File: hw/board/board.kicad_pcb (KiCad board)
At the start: 4 copper layers, 100 x 85 mm, 12 parts, among them J1 DE9_Receptacle, J2 DE9_Receptacle, J3 DE9_Receptacle, J4 DE9_Receptacle, J5 DE9_Receptacle, J6 DE9_Receptacle, J7 DE9_Receptacle, J8 DE9_Receptacle, U1 XC7A35T-FTG256

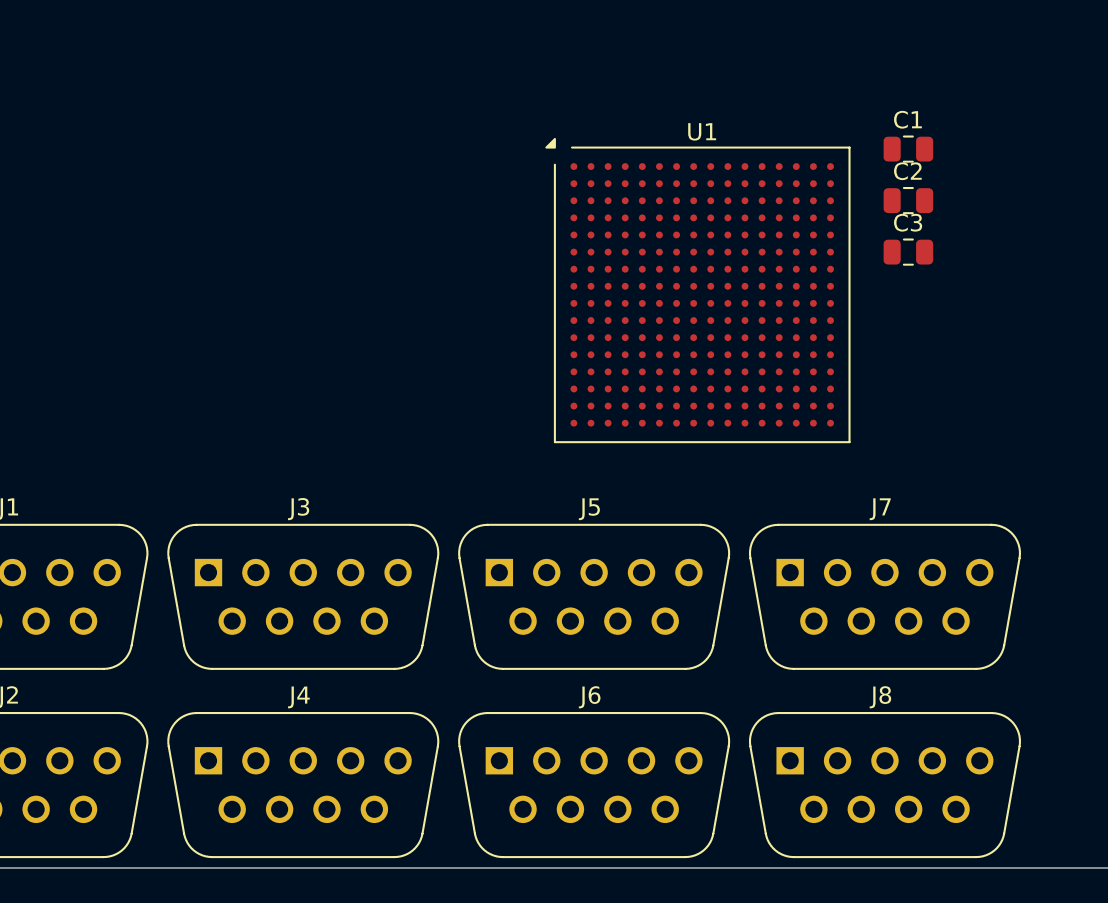
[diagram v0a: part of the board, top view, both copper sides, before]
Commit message: Added decoupling network following Xiling UG483
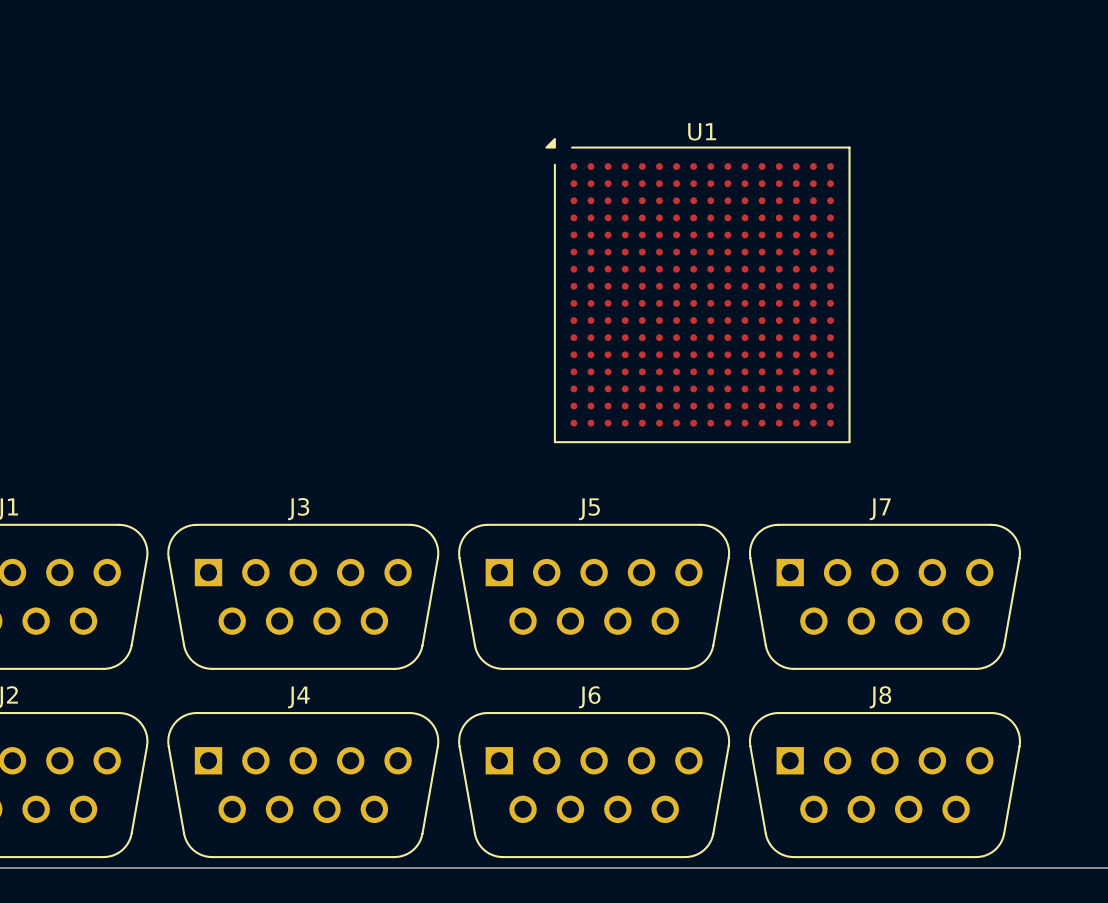
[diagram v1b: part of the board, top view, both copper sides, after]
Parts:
- removed C1, C2, C3: 10u, Capacitor_SMD:C_0805_2012Metric

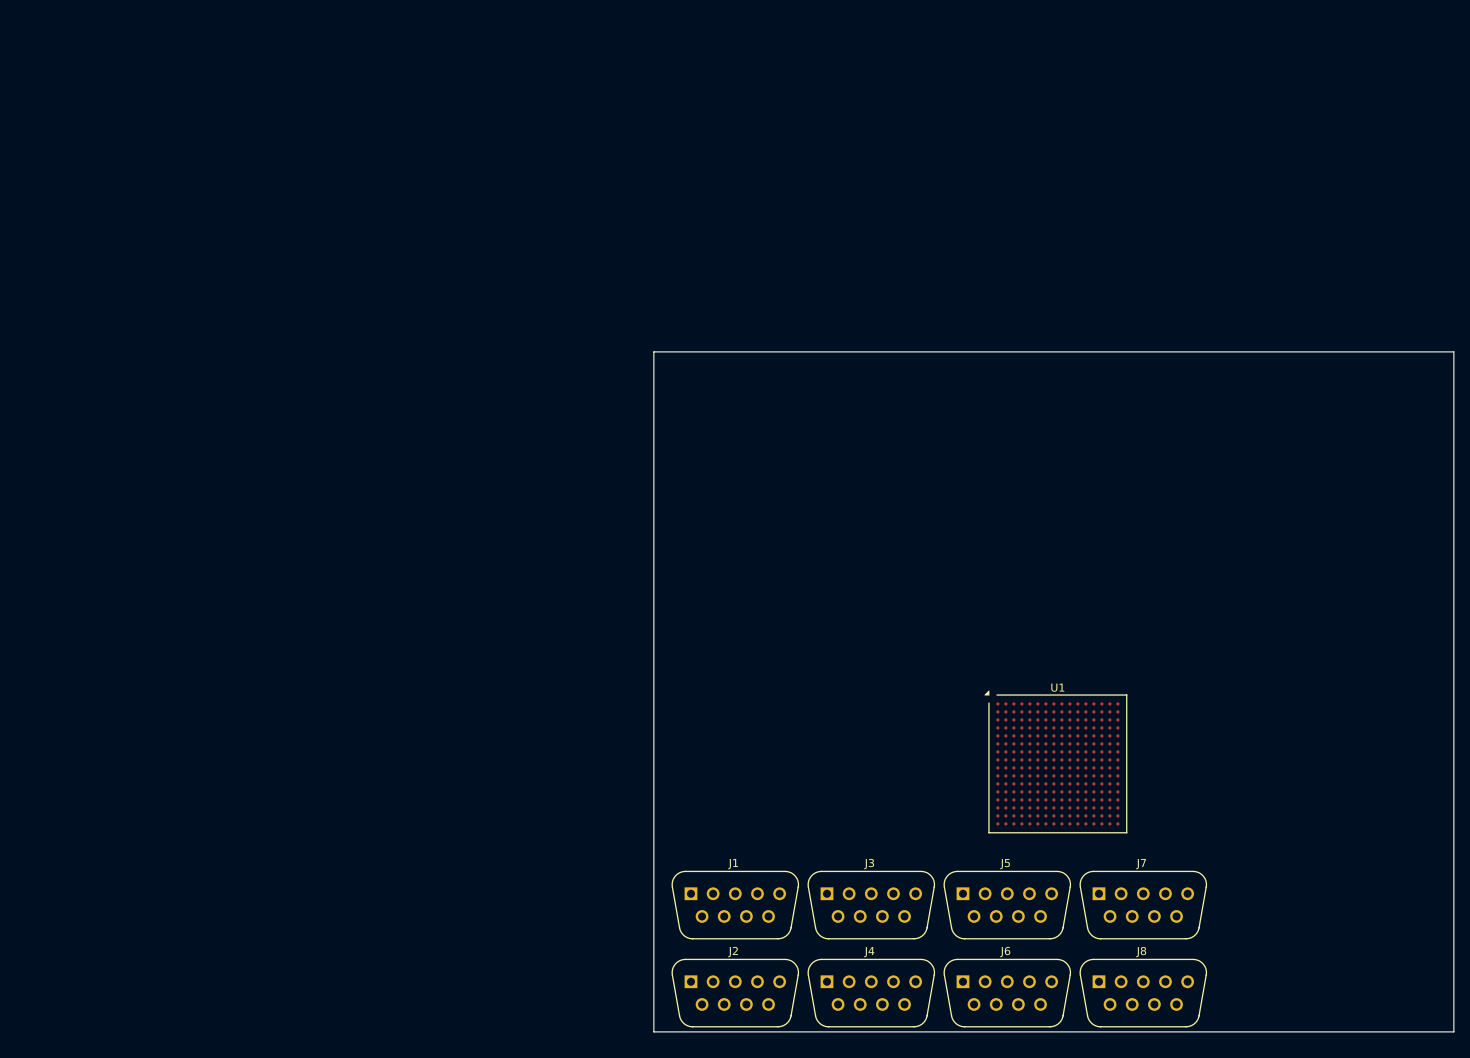
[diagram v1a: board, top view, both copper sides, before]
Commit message: Added DE9 connector footprint
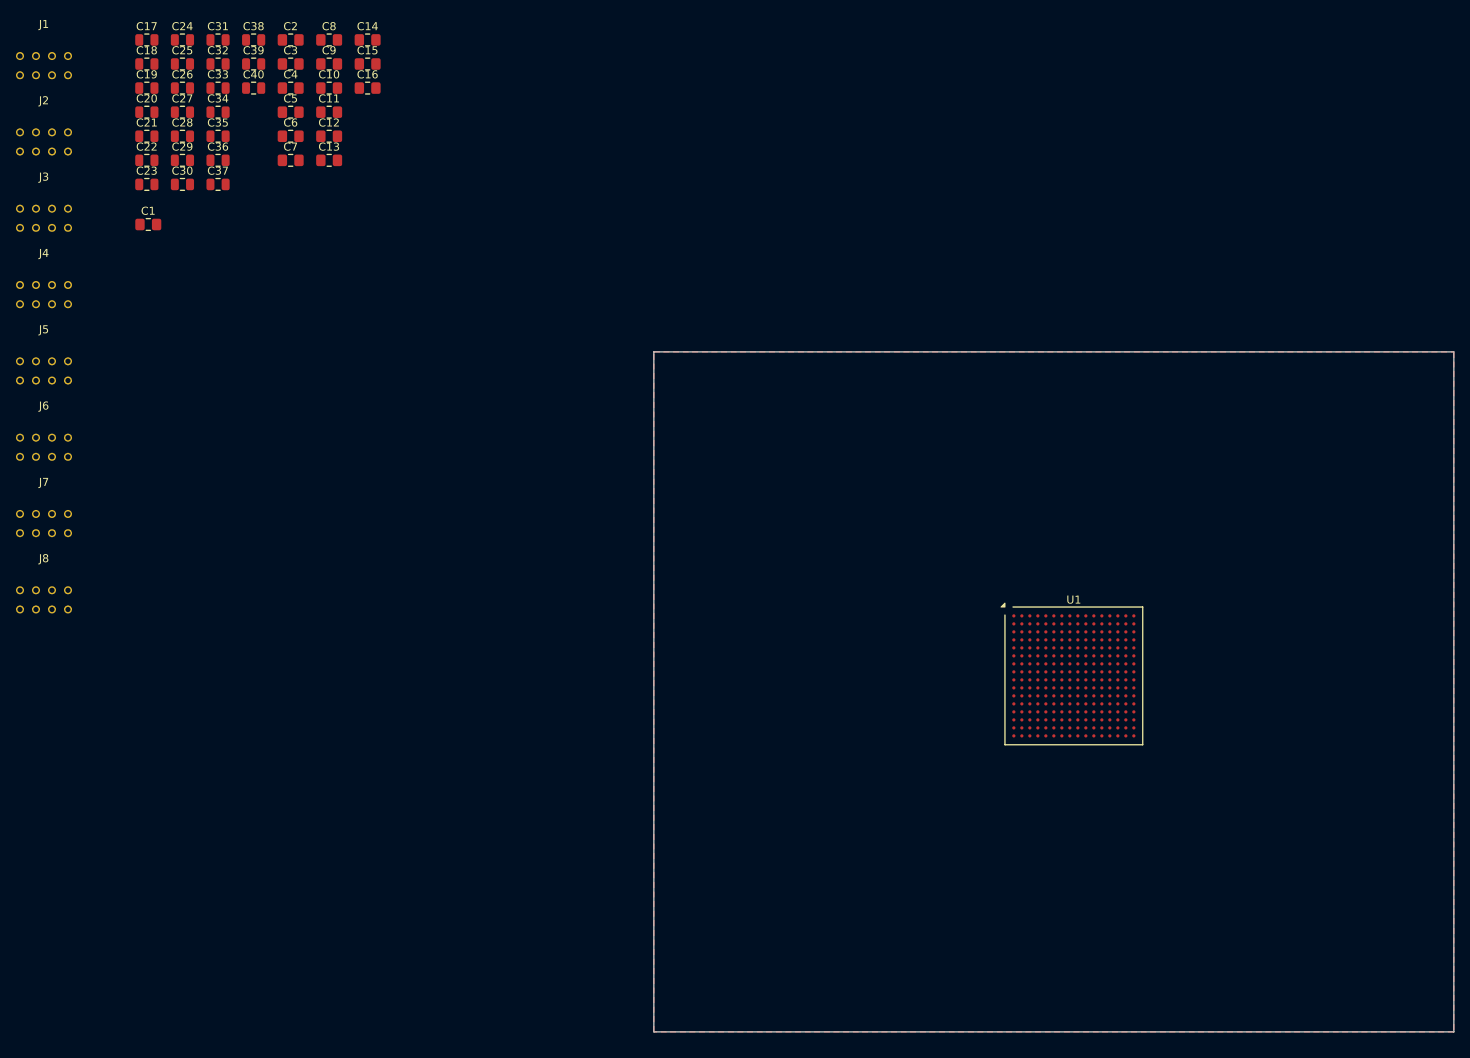
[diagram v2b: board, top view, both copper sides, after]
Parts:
- added C1: 47u, Capacitor_SMD:C_0805_2012Metric_Pad1.18x1.45mm_HandSolder, F.Cu at (20.8, 24.1)
- added C10: 100u, Capacitor_SMD:C_0805_2012Metric_Pad1.18x1.45mm_HandSolder, F.Cu at (43.4, 7.03)
- added C11: 4u7, Capacitor_SMD:C_0805_2012Metric_Pad1.18x1.45mm_HandSolder, F.Cu at (43.4, 10.0)
- added C12: 4u7, Capacitor_SMD:C_0805_2012Metric_Pad1.18x1.45mm_HandSolder, F.Cu at (43.4, 13.0)
- added C13: 470n, Capacitor_SMD:C_0805_2012Metric_Pad1.18x1.45mm_HandSolder, F.Cu at (43.4, 16.1)
- added C14: 470n, Capacitor_SMD:C_0805_2012Metric_Pad1.18x1.45mm_HandSolder, F.Cu at (48.2, 1.00)
- added C15: 470n, Capacitor_SMD:C_0805_2012Metric_Pad1.18x1.45mm_HandSolder, F.Cu at (48.2, 4.01)
- added C16: 100u, Capacitor_SMD:C_0805_2012Metric_Pad1.18x1.45mm_HandSolder, F.Cu at (48.2, 7.03)
- added C17: 470n, Capacitor_SMD:C_0805_2012Metric, F.Cu at (20.6, 1.00)
- added C18: 470n, Capacitor_SMD:C_0805_2012Metric, F.Cu at (20.6, 4.01)
- added C19: 470n, Capacitor_SMD:C_0805_2012Metric, F.Cu at (20.6, 7.03)
- added C2: 470n, Capacitor_SMD:C_0805_2012Metric_Pad1.18x1.45mm_HandSolder, F.Cu at (38.6, 1.00)
- added C20: 470n, Capacitor_SMD:C_0805_2012Metric, F.Cu at (20.6, 10.0)
- added C21: 4u7, Capacitor_SMD:C_0805_2012Metric, F.Cu at (20.6, 13.0)
- added C22: 4u7, Capacitor_SMD:C_0805_2012Metric, F.Cu at (20.6, 16.1)
- added C23: 4u7, Capacitor_SMD:C_0805_2012Metric, F.Cu at (20.6, 19.1)
- added C24: 4u7, Capacitor_SMD:C_0805_2012Metric, F.Cu at (25.1, 1.00)
- added C25: 470n, Capacitor_SMD:C_0805_2012Metric, F.Cu at (25.1, 4.01)
- added C26: 470n, Capacitor_SMD:C_0805_2012Metric, F.Cu at (25.1, 7.03)
- added C27: 470n, Capacitor_SMD:C_0805_2012Metric, F.Cu at (25.1, 10.0)
- added C28: 470n, Capacitor_SMD:C_0805_2012Metric, F.Cu at (25.1, 13.0)
- added C29: 470n, Capacitor_SMD:C_0805_2012Metric, F.Cu at (25.1, 16.1)
- added C3: 470n, Capacitor_SMD:C_0805_2012Metric_Pad1.18x1.45mm_HandSolder, F.Cu at (38.6, 4.01)
- added C30: 470n, Capacitor_SMD:C_0805_2012Metric, F.Cu at (25.1, 19.1)
- added C31: 470n, Capacitor_SMD:C_0805_2012Metric, F.Cu at (29.5, 1.00)
- added C32: 470n, Capacitor_SMD:C_0805_2012Metric, F.Cu at (29.5, 4.01)
- added C33: 4u7, Capacitor_SMD:C_0805_2012Metric, F.Cu at (29.5, 7.03)
- added C34: 4u7, Capacitor_SMD:C_0805_2012Metric, F.Cu at (29.5, 10.0)
- added C35: 4u7, Capacitor_SMD:C_0805_2012Metric, F.Cu at (29.5, 13.0)
- added C36: 4u7, Capacitor_SMD:C_0805_2012Metric, F.Cu at (29.5, 16.1)
- added C37: 470n, Capacitor_SMD:C_0805_2012Metric, F.Cu at (29.5, 19.1)
- added C38: 470n, Capacitor_SMD:C_0805_2012Metric, F.Cu at (34.0, 1.00)
- added C39: 470n, Capacitor_SMD:C_0805_2012Metric, F.Cu at (34.0, 4.01)
- added C4: 470n, Capacitor_SMD:C_0805_2012Metric_Pad1.18x1.45mm_HandSolder, F.Cu at (38.6, 7.03)
- added C40: 470n, Capacitor_SMD:C_0805_2012Metric, F.Cu at (34.0, 7.03)
- added C5: 4u7, Capacitor_SMD:C_0805_2012Metric_Pad1.18x1.45mm_HandSolder, F.Cu at (38.6, 10.0)
- added C6: 47u, Capacitor_SMD:C_0805_2012Metric_Pad1.18x1.45mm_HandSolder, F.Cu at (38.6, 13.0)
- added C7: 4u7, Capacitor_SMD:C_0805_2012Metric_Pad1.18x1.45mm_HandSolder, F.Cu at (38.6, 16.1)
- added C8: 470n, Capacitor_SMD:C_0805_2012Metric_Pad1.18x1.45mm_HandSolder, F.Cu at (43.4, 1.00)
- added C9: 47u, Capacitor_SMD:C_0805_2012Metric_Pad1.18x1.45mm_HandSolder, F.Cu at (43.4, 4.01)
- J1, J2, J3, J4, J5, J6, J7, J8: value DE9_Receptacle -> ~
- moved J8 145.8 mm to (7.77, 70.9)
- moved J7 145.3 mm to (7.77, 61.4)
- moved J6 138.2 mm to (7.77, 51.8)
- moved J5 137.5 mm to (7.77, 42.3)
- moved J2 136.9 mm to (7.77, 13.7)
- moved J1 135.8 mm to (7.77, 4.12)
- moved J4 135.2 mm to (7.77, 32.7)
- moved J3 134.2 mm to (7.77, 23.2)
- moved U1 11.2 mm to (136.5, 80.5)
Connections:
- U1 pad A1: Net-(U1D-GND-PadA1) -> GND
- U1 pad A11: Net-(U1D-GND-PadA1) -> GND
- U1 pad A16: unconnected-(U1A-VCCO_15-PadA16) -> +2V5
- U1 pad A6: unconnected-(U1B-VCCO_35-PadA6) -> +2V5
- U1 pad B13: unconnected-(U1A-VCCO_15-PadB13) -> +2V5
- U1 pad B3: unconnected-(U1B-VCCO_35-PadB3) -> +2V5
- U1 pad B8: Net-(U1D-GND-PadA1) -> GND
- U1 pad C10: unconnected-(U1A-VCCO_15-PadC10) -> +2V5
- U1 pad C15: Net-(U1D-GND-PadA1) -> GND
- U1 pad C5: Net-(U1D-GND-PadA1) -> GND
- U1 pad D12: Net-(U1D-GND-PadA1) -> GND
- U1 pad D2: Net-(U1D-GND-PadA1) -> GND
- U1 pad D7: unconnected-(U1B-VCCO_35-PadD7) -> +2V5
- U1 pad E14: unconnected-(U1A-VCCO_15-PadE14) -> +2V5
- U1 pad E4: unconnected-(U1B-VCCO_35-PadE4) -> +2V5
- U1 pad E7: +3V3 -> +2V5
- U1 pad E9: Net-(U1D-GND-PadA1) -> GND
- U1 pad F1: unconnected-(U1B-VCCO_35-PadF1) -> +2V5
- U1 pad F10: Net-(U1D-GND-PadA1) -> GND
- U1 pad F16: Net-(U1D-GND-PadA1) -> GND
- U1 pad F6: Net-(U1D-GND-PadA1) -> GND
- U1 pad F7: unconnected-(U1D-VCCINT-PadF7) -> +1V0
- U1 pad F8: unconnected-(U1D-VCCBATT_0-PadF8) -> GND
- U1 pad F9: unconnected-(U1D-VCCINT-PadF9) -> +1V0
- U1 pad G10: unconnected-(U1D-VCCAUX-PadG10) -> +1V8
- U1 pad G13: Net-(U1D-GND-PadA1) -> GND
- U1 pad G3: Net-(U1D-GND-PadA1) -> GND
- U1 pad G6: unconnected-(U1D-VCCINT-PadG6) -> +1V0
- U1 pad G7: unconnected-(U1D-GNDADC_0-PadG7) -> GND
- U1 pad G8: unconnected-(U1D-VCCADC_0-PadG8) -> GND
- U1 pad G9: Net-(U1D-GND-PadA1) -> GND
- U1 pad H15: unconnected-(U1A-VCCO_15-PadH15) -> +2V5
- U1 pad H6: Net-(U1D-GND-PadA1) -> GND
- U1 pad H9: unconnected-(U1D-VCCINT-PadH9) -> +1V0
- U1 pad J10: unconnected-(U1D-VCCAUX-PadJ10) -> +1V8
- U1 pad J11: Net-(U1D-GND-PadJ11) -> GND
- U1 pad J12: unconnected-(U1A-VCCO_15-PadJ12) -> +2V5
- U1 pad J2: unconnected-(U1B-VCCO_35-PadJ2) -> +2V5
- U1 pad J6: unconnected-(U1D-VCCINT-PadJ6) -> +1V0
- U1 pad J9: Net-(U1D-GND-PadJ11) -> GND
- U1 pad K11: unconnected-(U1D-VCCAUX-PadK11) -> +1V8
- U1 pad K14: Net-(U1D-GND-PadJ11) -> GND
- U1 pad K4: Net-(U1D-GND-PadJ11) -> GND
- U1 pad K6: Net-(U1D-GND-PadJ11) -> GND
- U1 pad K9: unconnected-(U1D-VCCINT-PadK9) -> +1V0
- U1 pad L1: Net-(U1D-GND-PadJ11) -> GND
- U1 pad L10: unconnected-(U1D-VCCAUX-PadL10) -> +1V8
- U1 pad L11: Net-(U1D-GND-PadJ11) -> GND
- U1 pad L16: unconnected-(U1A-VCCO_14-PadL16) -> +2V5
- U1 pad L6: +3V3 -> +2V5
- U1 pad L8: unconnected-(U1D-VCCINT-PadL8) -> +1V0
- U1 pad M13: unconnected-(U1A-VCCO_14-PadM13) -> +2V5
- U1 pad M3: +3V3 -> +2V5
- U1 pad M8: Net-(U1D-GND-PadJ11) -> GND
- U1 pad N10: unconnected-(U1A-VCCO_14-PadN10) -> +2V5
- U1 pad N15: Net-(U1D-GND-PadJ11) -> GND
- U1 pad N5: Net-(U1D-GND-PadJ11) -> GND
- U1 pad P12: Net-(U1D-GND-PadJ11) -> GND
- U1 pad P2: Net-(U1D-GND-PadJ11) -> GND
- U1 pad P7: unconnected-(U1A-VCCO_14-PadP7) -> +2V5
- U1 pad R14: unconnected-(U1A-VCCO_14-PadR14) -> +2V5
- U1 pad R4: +3V3 -> +2V5
- U1 pad R9: Net-(U1D-GND-PadJ11) -> GND
- U1 pad T1: +3V3 -> +2V5
- U1 pad T11: unconnected-(U1A-VCCO_14-PadT11) -> +2V5
- U1 pad T16: Net-(U1D-GND-PadJ11) -> GND
- U1 pad T6: Net-(U1D-GND-PadJ11) -> GND
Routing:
- added copper zone on F.Cu, net GND
- added copper zone on In1.Cu, net GND
- added copper zone on In2.Cu, net GND
